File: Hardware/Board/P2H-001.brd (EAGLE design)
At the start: 47 x 72 mm, 14 parts, among them IC1 74LS07N, IC2 LTC485N

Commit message: New board design.
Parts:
- added LED1: (no value), led:LED3MM
- added R5: 330, resistor:0204/5
- moved JP4 5.08 mm to (26.7, 30.5)
- moved JP2 5.08 mm to (15.2, 30.5)
- moved R1 2.54 mm to (36.8, 44.5)
- moved R2 2.54 mm to (36.8, 36.8)
- moved R3 2.54 mm to (36.8, 52.1)
- moved R4 2.54 mm to (34.3, 31.8)
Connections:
- new net N$20: R5.2, U$1.8
- new net N$21: LED1.A, R5.1
- net GND: now also LED1.K
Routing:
- net N$21: track 0.00 -> 27.4 mm
- net N$20: track 0.00 -> 15.9 mm
- net N$4: track 36.8 -> 50.1 mm
- net N$13: track 45.7 -> 34.2 mm
- net N$15: track 40.2 -> 29.3 mm
- net N$17: track 34.7 -> 25.8 mm
- net GND: track 137.0 -> 144.2 mm
- net N$12: track 19.9 -> 26.5 mm
- net N$10: track 31.7 -> 37.8 mm
- net N$6: track 28.7 -> 32.8 mm
- net N$16: track 32.5 -> 28.5 mm
- net N$1: track 55.2 -> 52.5 mm, vias 1 -> 0
- net N$5: track 16.2 -> 13.6 mm
- net N$7: track 14.8 -> 12.3 mm
- net N$18: track 22.5 -> 20.0 mm
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
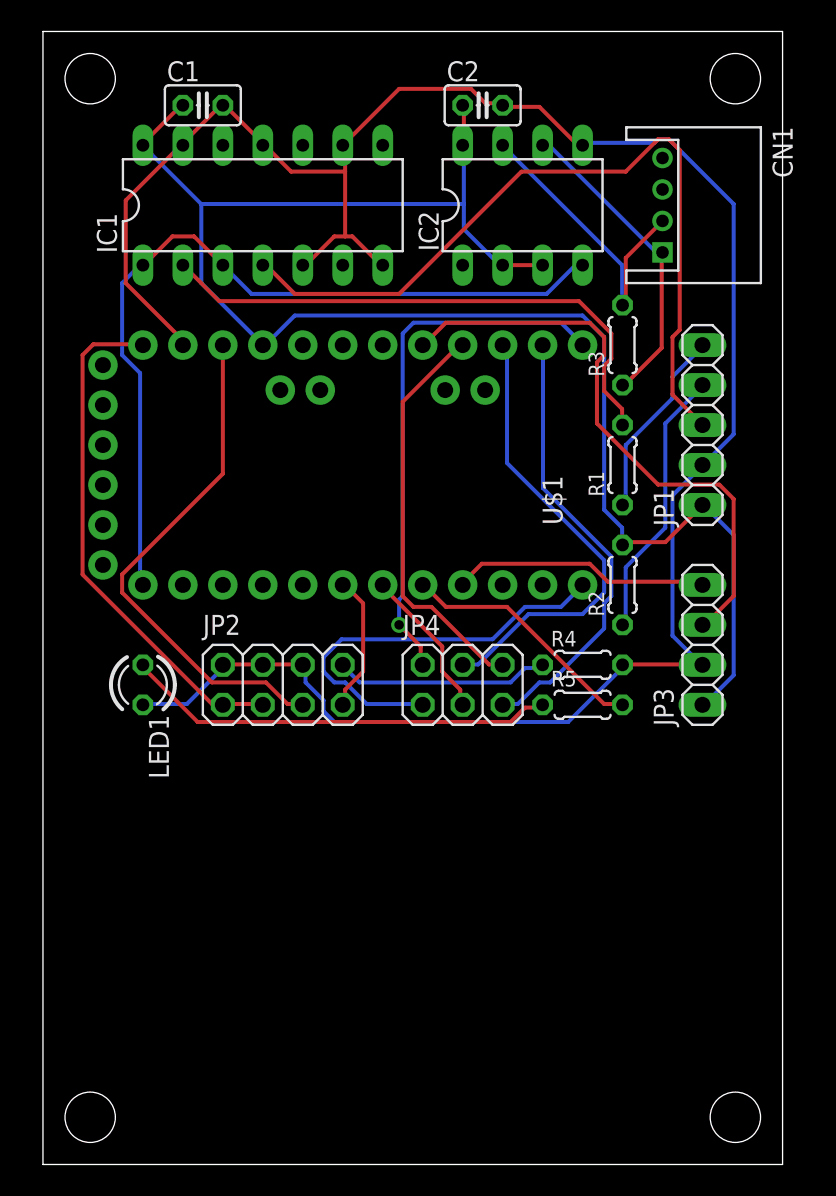
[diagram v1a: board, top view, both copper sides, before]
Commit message: Changed board size to 45mm x 45mm.
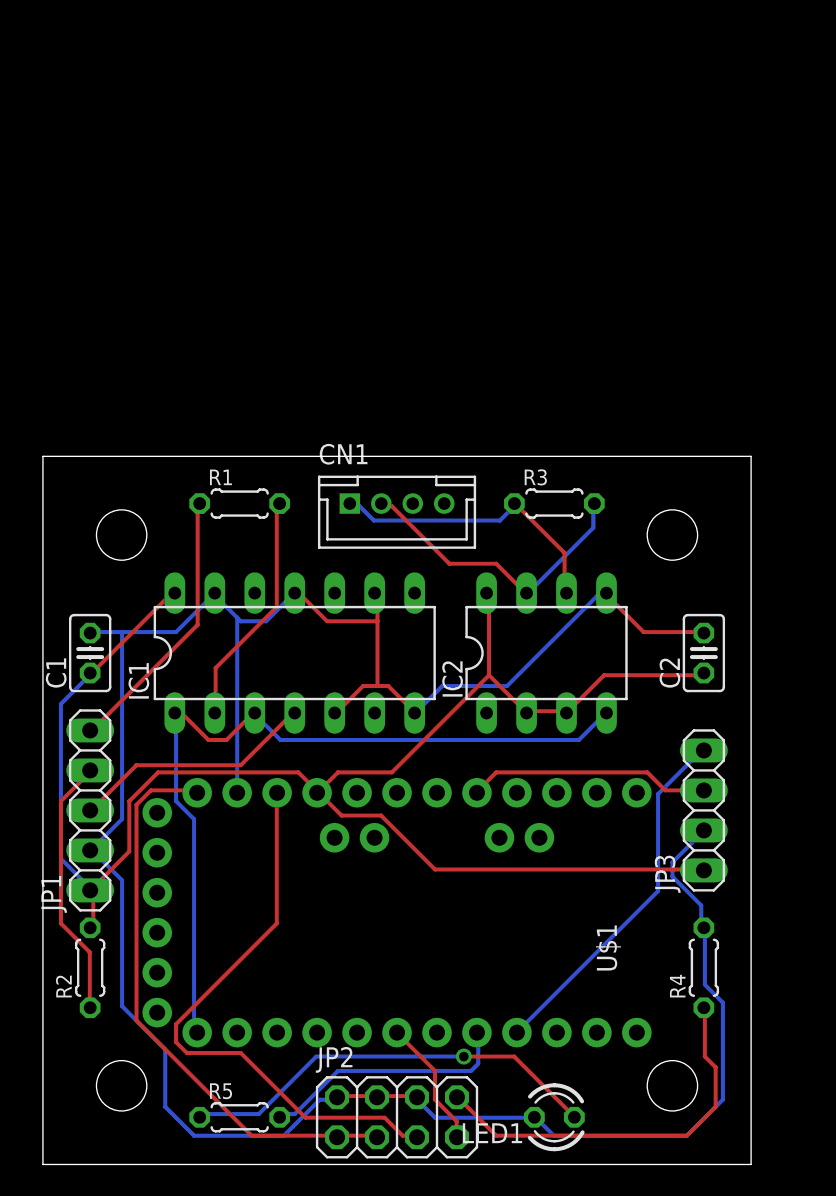
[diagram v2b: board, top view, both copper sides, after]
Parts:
- removed JP4: (no value), pinhead:2X03
- CN1: device jst-ph:S4B-PH-K-S -> jst-ph:B4B-PH-K-S
- moved JP1 46.0 mm to (3.00, 22.5)
- moved R2 41.7 mm to (3.00, 12.5)
- moved LED1 37.9 mm to (32.5, 3.00), turned to 180 degrees
- moved C2 37.5 mm to (42.0, 32.5), turned to 90 degrees
- moved C1 35.5 mm to (3.00, 32.5), turned to 90 degrees
- moved R5 34.1 mm to (12.5, 3.00)
- moved U$1 28.7 mm to (22.5, 16.0)
- moved IC1 28.5 mm to (16.0, 32.5)
- moved IC2 28.5 mm to (32.0, 32.5)
- moved JP2 28.4 mm to (22.5, 3.00)
- moved CN1 25.4 mm to (22.5, 42.0), turned to 0 degrees
- moved R1 24.5 mm to (12.5, 42.0), turned to 0 degrees
- moved R4 20.7 mm to (42.0, 12.5), turned to 90 degrees
- moved R3 11.0 mm to (32.5, 42.0), turned to 0 degrees
- moved JP3 10.5 mm to (42.0, 22.5)
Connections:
- removed net N$12: JP4.1, U$1.12
- removed net N$13: JP4.2, U$1.13
- removed net N$14: JP4.3, U$1.7
- removed net N$15: JP4.4, U$1.15
- removed net N$16: JP4.5, U$1.14
- removed net N$17: JP4.6, U$1.16
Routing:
- net N$4: track 50.1 -> 15.5 mm
- net N$13: track 34.2 -> 0.00 mm, vias 1 -> 0
- net N$15: track 29.3 -> 0.00 mm
- net N$16: track 28.5 -> 0.00 mm
- net N$12: track 26.5 -> 0.00 mm
- net N$17: track 25.8 -> 0.00 mm
- net N$10: track 37.8 -> 15.5 mm
- net N$2: track 35.5 -> 15.0 mm
- net GND: track 144.2 -> 159.6 mm
- net N$5: track 13.6 -> 24.8 mm
- net N$14: track 9.89 -> 0.00 mm
- net N$11: track 16.5 -> 22.9 mm
- net N$7: track 12.3 -> 17.3 mm
- net N$6: track 32.8 -> 36.3 mm
- net N$9: track 33.0 -> 36.4 mm
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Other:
- board size 47 x 72 mm -> 45 x 45 mm
- board text removed: "PINEAPPLE II HYDROGEN REVISION 1.0.0 (2015)"

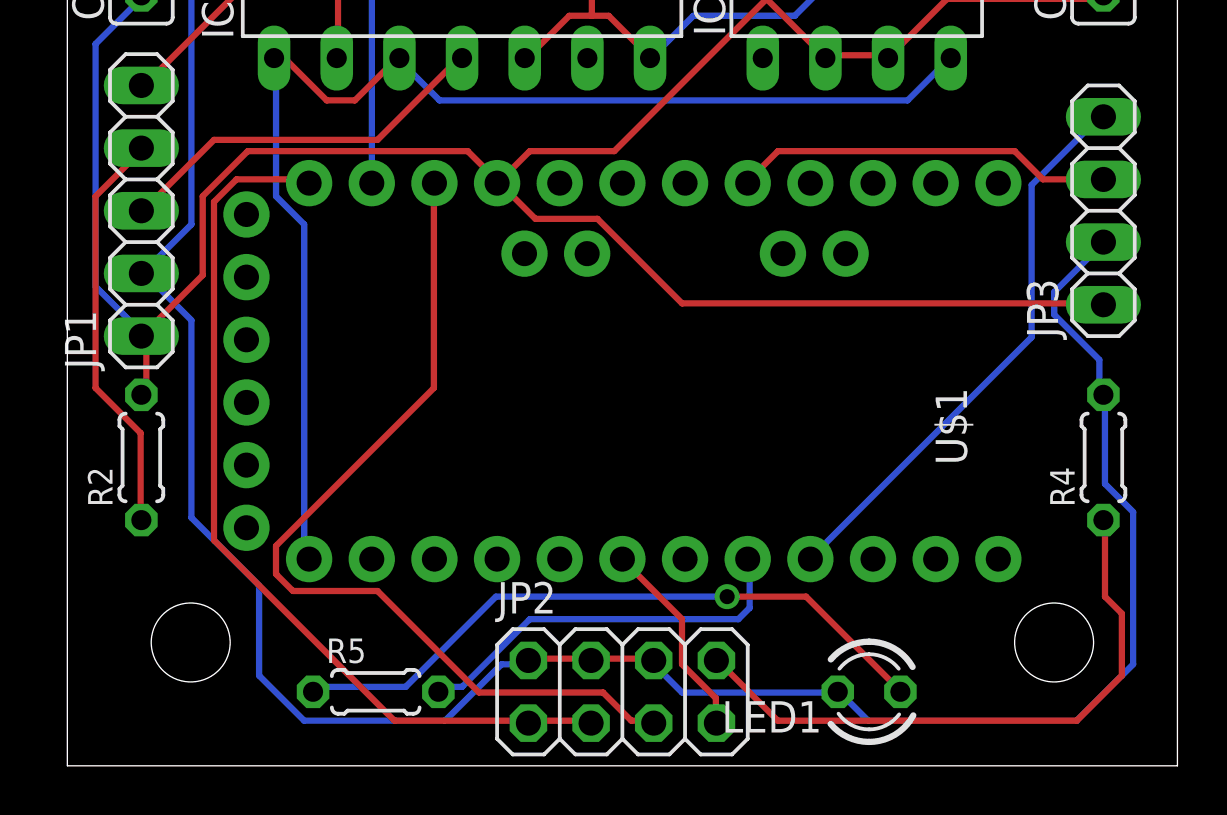
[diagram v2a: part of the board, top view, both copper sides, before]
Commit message: Changed position of LED resistor.
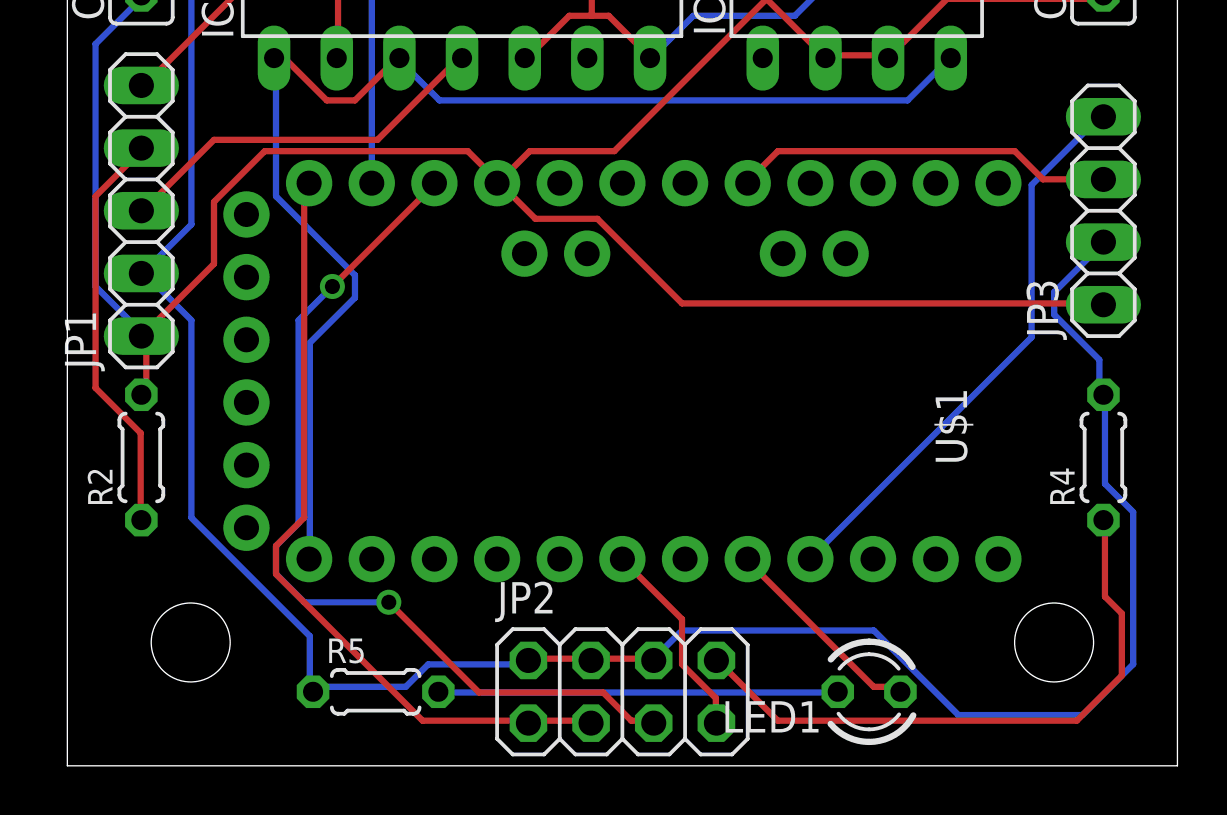
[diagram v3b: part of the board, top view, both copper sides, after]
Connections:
- removed net N$20: R5.2, U$1.8
- removed net N$21: LED1.A, R5.1
- new net N$12: LED1.A, U$1.8
- new net N$13: LED1.K, R5.2
- net GND: now also R5.1; no longer LED1.K
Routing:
- net N$21: track 27.1 -> 0.00 mm, vias 1 -> 0
- net N$13: track 0.00 -> 16.2 mm
- net N$20: track 16.1 -> 0.00 mm
- net N$12: track 0.00 -> 8.46 mm
- net N$9: track 36.4 -> 31.8 mm
- net N$1: track 51.2 -> 52.7 mm
- net GND: track 159.6 -> 158.6 mm
- net N$6: vias 0 -> 2

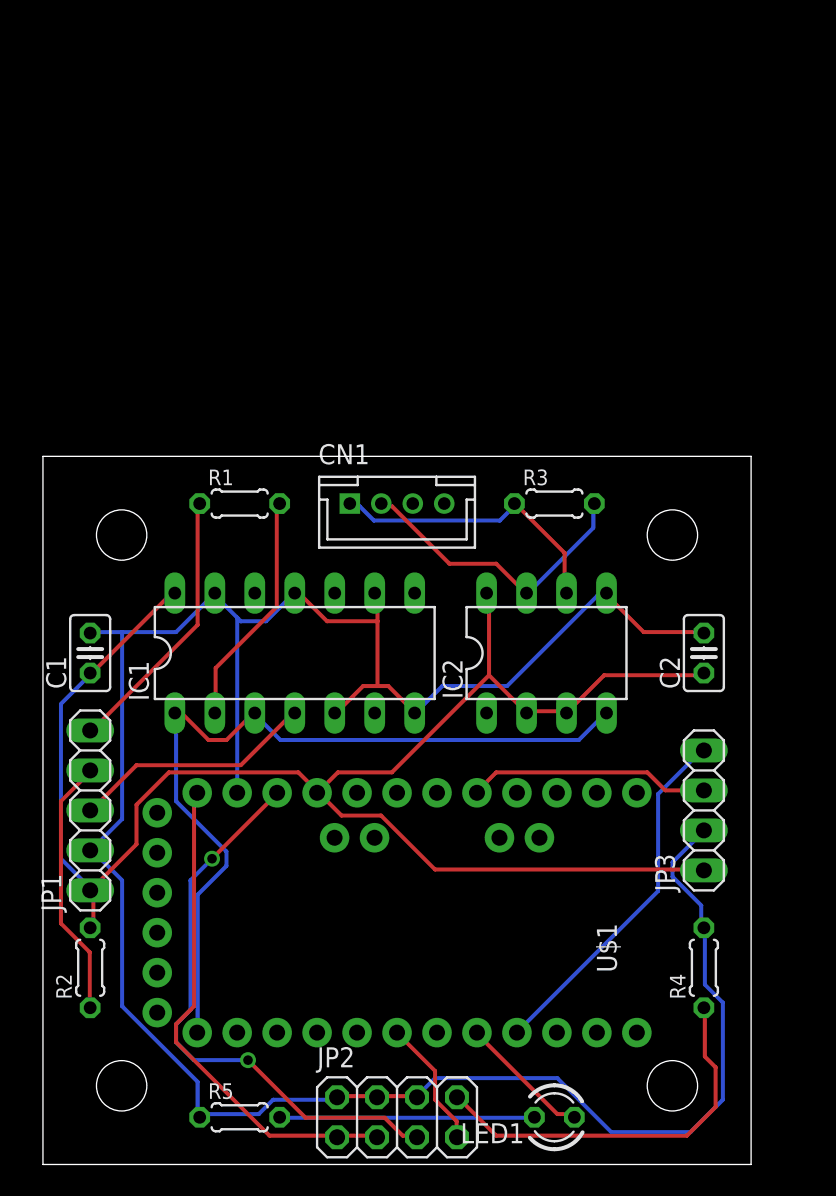
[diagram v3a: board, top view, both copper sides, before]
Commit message: Adopted to the new pinout.
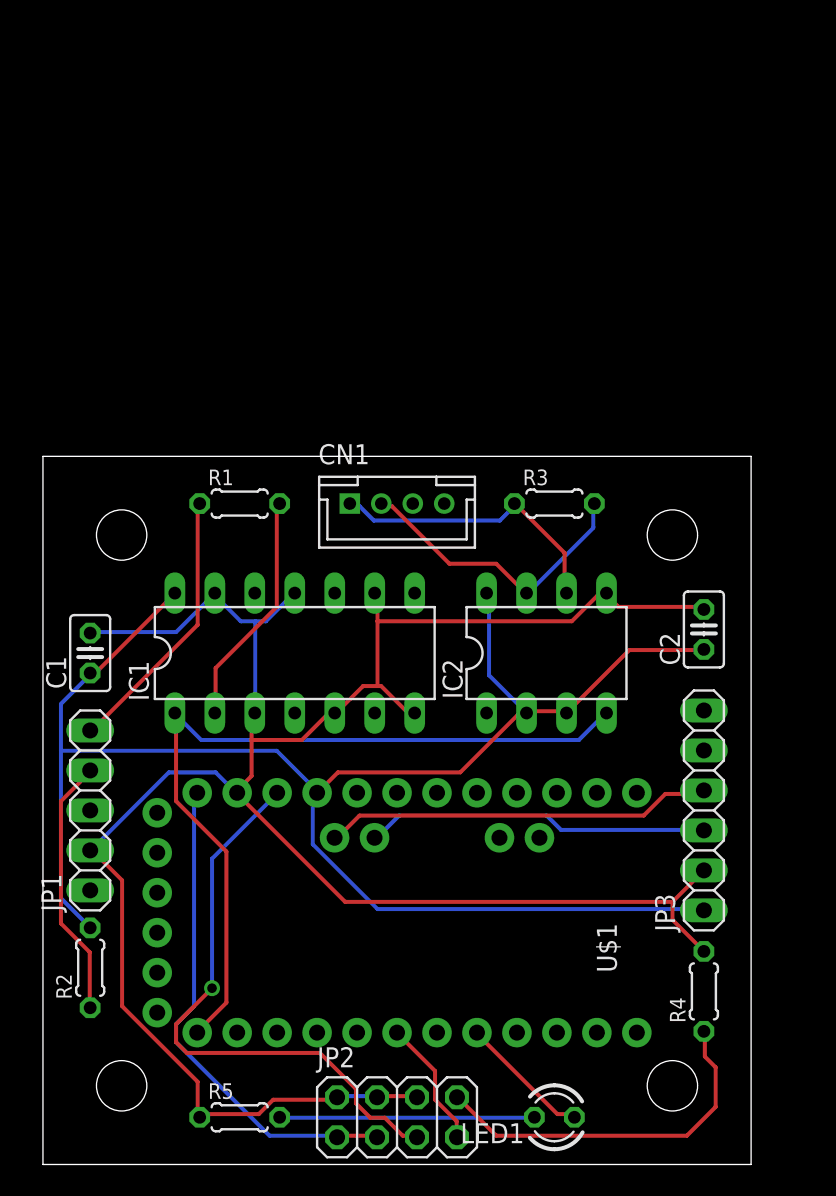
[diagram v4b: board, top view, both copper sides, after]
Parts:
- JP3: device pinhead:1X04 -> pinhead:1X06
- moved C2 1.50 mm to (42.0, 34.0)
- moved R4 1.50 mm to (42.0, 11.0)
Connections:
- removed net N$4: IC1.4, JP1.3
- net GND: now also IC1.3
- net N$1: no longer IC1.3
- net N$10: now also U$1.A4; no longer U$1.17
- net N$11: now also U$1.A5; no longer U$1.9
- net VCC: no longer JP1.1
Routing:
- net N$4: track 15.5 -> 0.00 mm
- net GND: track 158.6 -> 151.1 mm
- net N$10: track 15.5 -> 21.9 mm
- net VCC: track 106.8 -> 109.8 mm
- net N$11: track 22.9 -> 24.7 mm
- net N$5: track 24.8 -> 23.3 mm
- net N$1: track 52.7 -> 51.3 mm
- net N$6: track 36.3 -> 36.8 mm, vias 2 -> 1
